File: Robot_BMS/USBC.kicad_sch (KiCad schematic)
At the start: 9 parts, among them IC2 STUSB4710AQTR, J1 632723300011

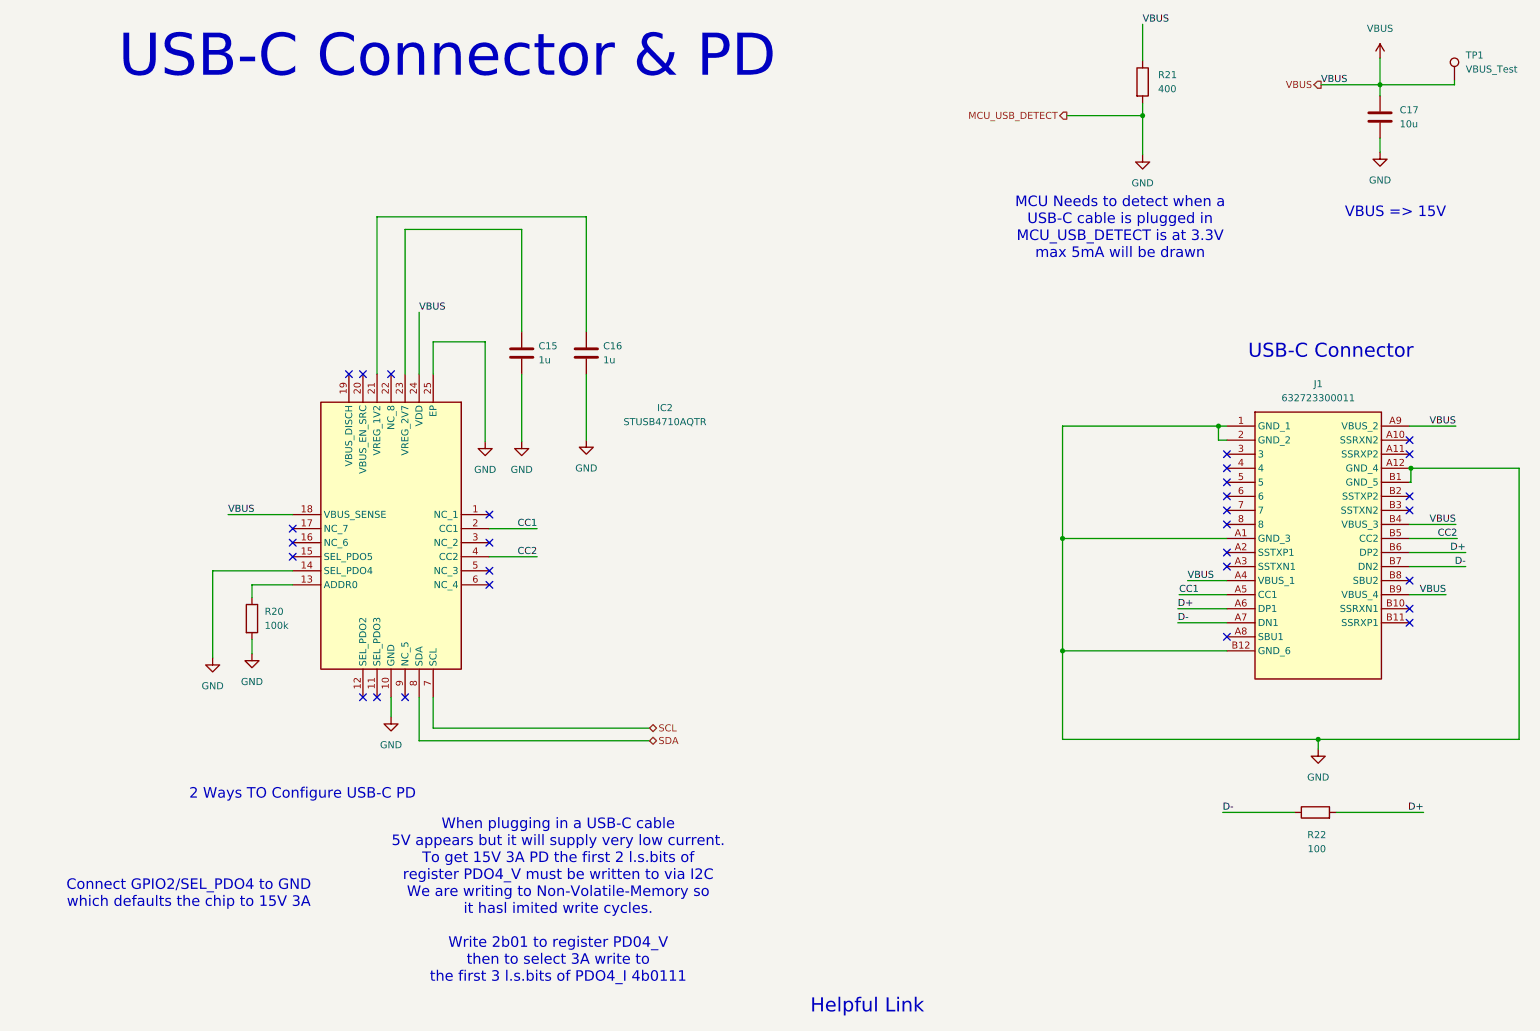
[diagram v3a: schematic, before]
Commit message: solar charger set to 15V
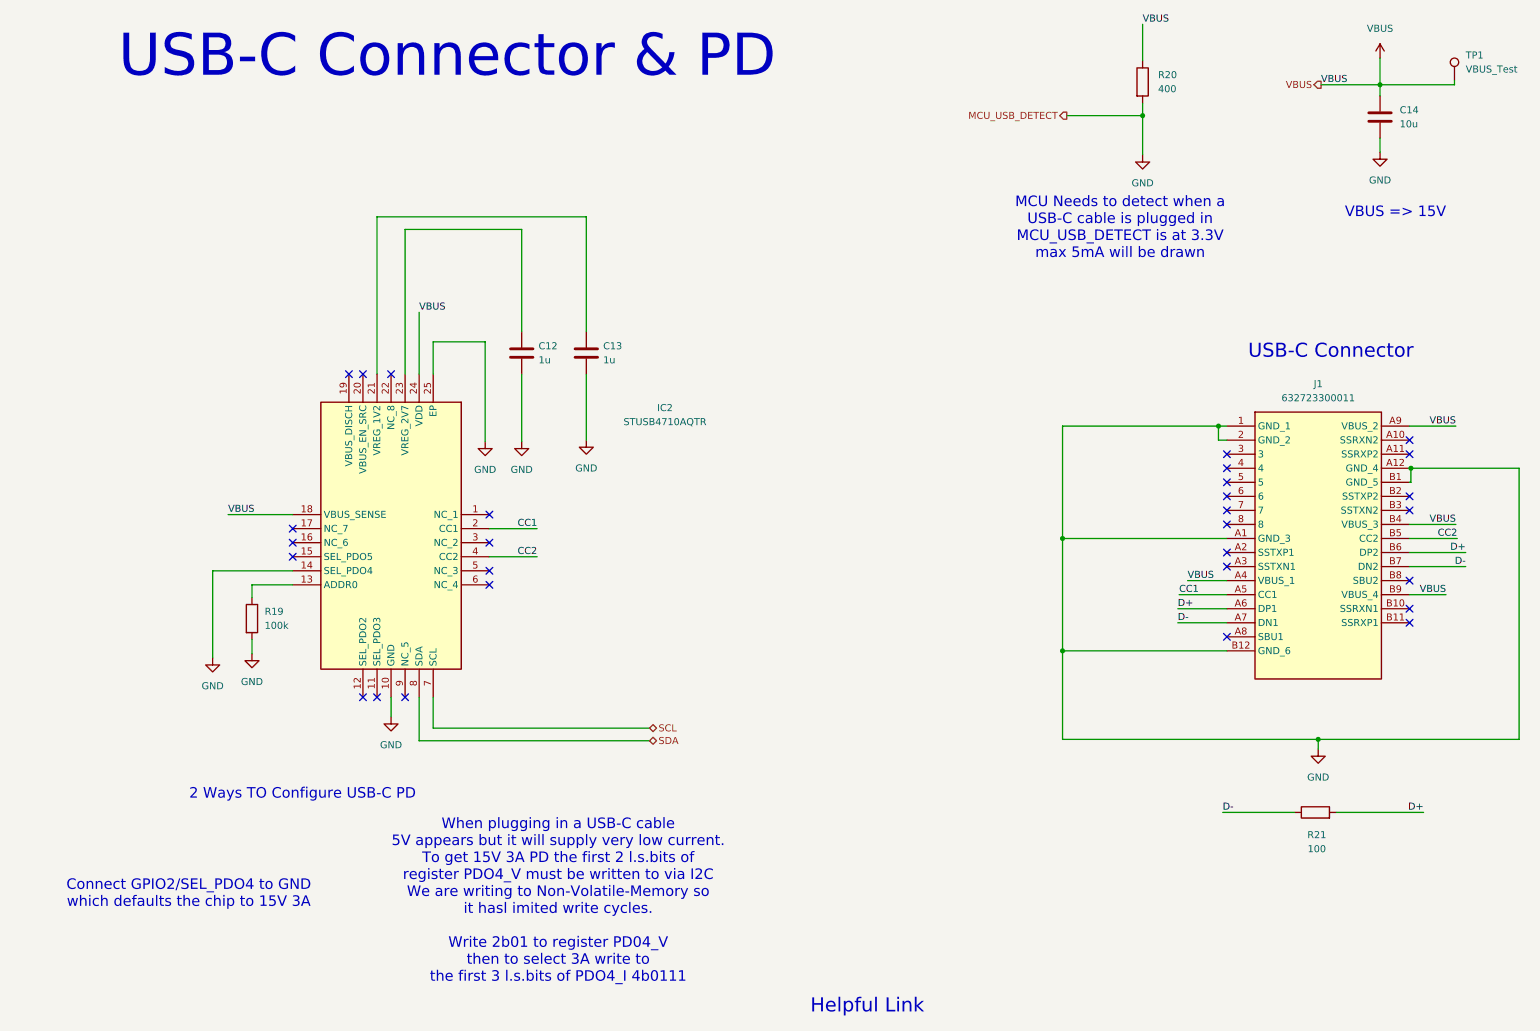
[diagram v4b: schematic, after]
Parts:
- renumbered C15 to C12, C16 to C13, C17 to C14, R20 to R19, R21 to R20, R22 to R21
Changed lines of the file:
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@@
 		(dnp no)
 		(fields_autoplaced yes)
-		(property "Reference" "#PWR011"
+		(property "Reference" "#PWR016"
 			(at 94.234 98.552 0)
 			(effects
@@
 			(project "Robot_BMS"
 				(path "/72551b1c-3d40-4199-8911-e5b015f4abec/c1bdabe1-a4b5-470d-80f8-90d5658c2a45"
-					(reference "#PWR011")
+					(reference "#PWR016")
 					(unit 1)
 				)
@@
 		(dnp no)
 		(fields_autoplaced yes)
-		(property "Reference" "#PWR09"
+		(property "Reference" "#PWR014"
 			(at 52.07 136.906 0)
 			(effects
@@
 			(project "Robot_BMS"
 				(path "/72551b1c-3d40-4199-8911-e5b015f4abec/c1bdabe1-a4b5-470d-80f8-90d5658c2a45"
-					(reference "#PWR09")
+					(reference "#PWR014")
 					(unit 1)
 				)
@@
 		(dnp no)
 		(fields_autoplaced yes)
-		(property "Reference" "#PWR013"
+		(property "Reference" "#PWR018"
 			(at 112.522 98.298 0)
 			(effects
@@
 			(project "Robot_BMS"
 				(path "/72551b1c-3d40-4199-8911-e5b015f4abec/c1bdabe1-a4b5-470d-80f8-90d5658c2a45"
-					(reference "#PWR013")
+					(reference "#PWR018")
 					(unit 1)
 				)
@@
 		(dnp no)
 		(fields_autoplaced yes)
-		(property "Reference" "#PWR035"
+		(property "Reference" "#PWR013"
 			(at 44.958 137.668 0)
 			(effects
@@
 			(project "Robot_BMS"
 				(path "/72551b1c-3d40-4199-8911-e5b015f4abec/c1bdabe1-a4b5-470d-80f8-90d5658c2a45"
-					(reference "#PWR035")
+					(reference "#PWR013")
 					(unit 1)
 				)
@@
 		(dnp no)
 		(fields_autoplaced yes)
-		(property "Reference" "#PWR010"
+		(property "Reference" "#PWR015"
 			(at 77.216 148.336 0)
 			(effects
@@
 			(project "Robot_BMS"
 				(path "/72551b1c-3d40-4199-8911-e5b015f4abec/c1bdabe1-a4b5-470d-80f8-90d5658c2a45"
-					(reference "#PWR010")
+					(reference "#PWR015")
 					(unit 1)
 				)
@@
 		(dnp no)
 		(fields_autoplaced yes)
-		(property "Reference" "C17"
+		(property "Reference" "C14"
 			(at 259.588 32.2579 0)
 			(effects
@@
 			(project "Robot_BMS"
 				(path "/72551b1c-3d40-4199-8911-e5b015f4abec/c1bdabe1-a4b5-470d-80f8-90d5658c2a45"
-					(reference "C17")
+					(reference "C14")
 					(unit 1)
 				)
@@
 		(dnp no)
 		(fields_autoplaced yes)
-		(property "Reference" "#PWR017"
+		(property "Reference" "#PWR022"
 			(at 256.032 46.228 0)
 			(effects
@@
 			(project "Robot_BMS"
 				(path "/72551b1c-3d40-4199-8911-e5b015f4abec/c1bdabe1-a4b5-470d-80f8-90d5658c2a45"
-					(reference "#PWR017")
+					(reference "#PWR022")
 					(unit 1)
 				)
@@
 		(dnp no)
 		(fields_autoplaced yes)
-		(property "Reference" "R21"
+		(property "Reference" "R20"
 			(at 215.9 25.9079 0)
 			(effects
@@
 			(project ""
 				(path "/72551b1c-3d40-4199-8911-e5b015f4abec/c1bdabe1-a4b5-470d-80f8-90d5658c2a45"
-					(reference "R21")
+					(reference "R20")
 					(unit 1)
 				)
@@
 		(dnp no)
 		(fields_autoplaced yes)
-		(property "Reference" "C16"
+		(property "Reference" "C13"
 			(at 115.57 74.9299 0)
 			(effects
@@
 			(project "Robot_BMS"
 				(path "/72551b1c-3d40-4199-8911-e5b015f4abec/c1bdabe1-a4b5-470d-80f8-90d5658c2a45"
-					(reference "C16")
+					(reference "C13")
 					(unit 1)
 				)
@@
 		(dnp no)
 		(fields_autoplaced yes)
-		(property "Reference" "#PWR012"
+		(property "Reference" "#PWR017"
 			(at 100.838 98.552 0)
 			(effects
@@
 			(project "Robot_BMS"
 				(path "/72551b1c-3d40-4199-8911-e5b015f4abec/c1bdabe1-a4b5-470d-80f8-90d5658c2a45"
-					(reference "#PWR012")
+					(reference "#PWR017")
 					(unit 1)
 				)
@@
 		(dnp no)
 		(fields_autoplaced yes)
-		(property "Reference" "R20"
+		(property "Reference" "R19"
 			(at 54.356 122.9359 0)
 			(effects
@@
 			(project ""
 				(path "/72551b1c-3d40-4199-8911-e5b015f4abec/c1bdabe1-a4b5-470d-80f8-90d5658c2a45"
-					(reference "R20")
+					(reference "R19")
 					(unit 1)
 				)
@@
 		(dnp no)
 		(fields_autoplaced yes)
-		(property "Reference" "#PWR015"
+		(property "Reference" "#PWR020"
 			(at 244.856 154.178 0)
 			(effects
@@
 			(project "Robot_BMS"
 				(path "/72551b1c-3d40-4199-8911-e5b015f4abec/c1bdabe1-a4b5-470d-80f8-90d5658c2a45"
-					(reference "#PWR015")
+					(reference "#PWR020")
 					(unit 1)
 				)
@@
 		(dnp no)
 		(fields_autoplaced yes)
-		(property "Reference" "#PWR016"
+		(property "Reference" "#PWR021"
 			(at 256.032 26.67 0)
 			(effects
@@
 			(project ""
 				(path "/72551b1c-3d40-4199-8911-e5b015f4abec/c1bdabe1-a4b5-470d-80f8-90d5658c2a45"
-					(reference "#PWR016")
+					(reference "#PWR021")
 					(unit 1)
 				)
@@
 		(on_board yes)
 		(dnp no)
-		(property "Reference" "R22"
+		(property "Reference" "R21"
 			(at 244.602 163.322 90)
 			(effects
@@
 			(project ""
 				(path "/72551b1c-3d40-4199-8911-e5b015f4abec/c1bdabe1-a4b5-470d-80f8-90d5658c2a45"
-					(reference "R22")
+					(reference "R21")
 					(unit 1)
 				)
@@
 		(dnp no)
 		(fields_autoplaced yes)
-		(property "Reference" "#PWR014"
+		(property "Reference" "#PWR019"
 			(at 213.106 46.736 0)
 			(effects
@@
 			(project "Robot_BMS"
 				(path "/72551b1c-3d40-4199-8911-e5b015f4abec/c1bdabe1-a4b5-470d-80f8-90d5658c2a45"
-					(reference "#PWR014")
+					(reference "#PWR019")
 					(unit 1)
 				)
@@
 		(dnp no)
 		(fields_autoplaced yes)
-		(property "Reference" "C15"
+		(property "Reference" "C12"
 			(at 103.886 74.9299 0)
 			(effects
@@
 			(project ""
 				(path "/72551b1c-3d40-4199-8911-e5b015f4abec/c1bdabe1-a4b5-470d-80f8-90d5658c2a45"
-					(reference "C15")
-					(unit 1)
-				)
+					(reference "C12")
+					(unit 1)
+				)
